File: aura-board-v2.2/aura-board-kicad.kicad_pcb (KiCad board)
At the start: 2 copper layers, 76.8 x 53.3 mm, 21 parts, among them J1 Power, J2 PWM, J3 BBCON, J4 Atto, J5 GPS, J6 SBUS, J7 Tele, J8 I2C0, U1 TSR2-2450, U2 PocketBeagle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

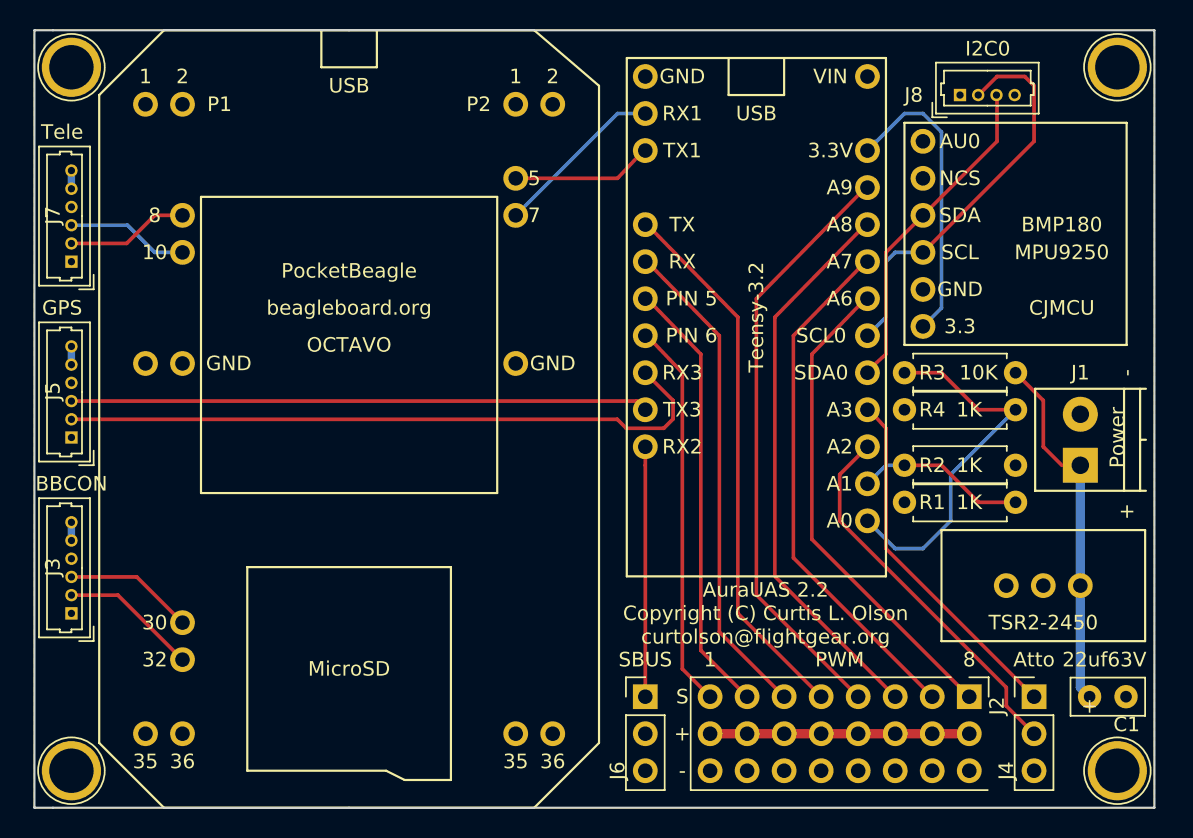
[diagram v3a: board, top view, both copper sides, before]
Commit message: Follow the standard drone-code pin order for external connectors. Fiddle with a couple traces to hopefully shorten and simplify.
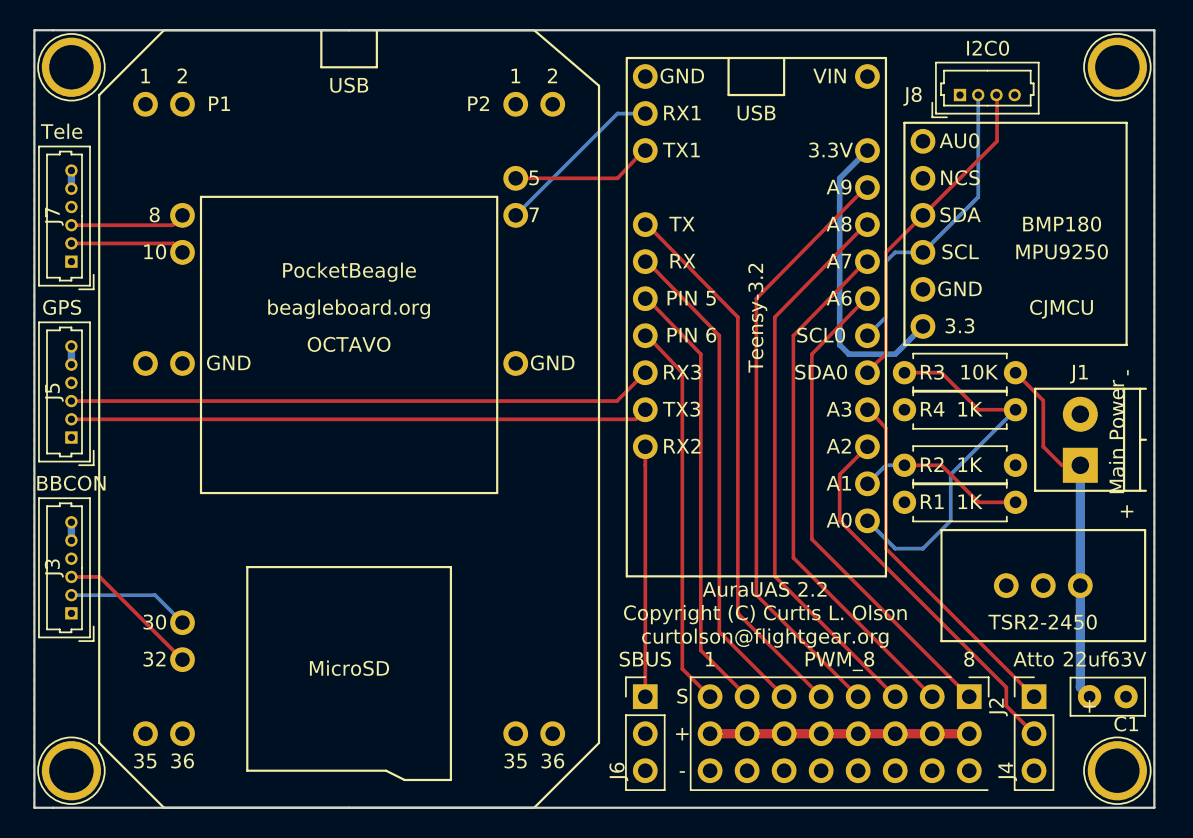
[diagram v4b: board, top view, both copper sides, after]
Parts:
- J1: value Power -> Main Power
- J2: value PWM -> PWM_8
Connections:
- J3 pad 2: /UART0_RX -> /UART0_TX
- J3 pad 3: /UART0_TX -> /UART0_RX
- J5 pad 2: /GPS_RX -> /GPS_TX
- J5 pad 3: /GPS_TX -> /GPS_RX
- J7 pad 2: /UART2_RX -> /UART2_TX
- J7 pad 3: /UART2_TX -> /UART2_RX
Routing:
- net /I2C0_SCL: track 27.6 -> 20.8 mm
- net /GPS_RX: track 45.9 -> 40.3 mm
- net /UART2_RX: track 8.42 -> 7.90 mm
- net /UART2_TX: track 8.39 -> 7.87 mm
- net /UART0_TX: track 8.92 -> 8.40 mm
- net /UART0_RX: track 9.45 -> 9.97 mm
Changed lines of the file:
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@@
     (thickness 1.6)
     (drawings 15)
-    (tracks 119)
+    (tracks 109)
     (zones 0)
     (modules 21)
@@
   )
   (setup
-    (last_trace_width 0.1524)
+    (last_trace_width 0.635)
     (user_trace_width 0.254)
     (user_trace_width 0.381)
@@
       (net 11 +5V))
     (pad 2 thru_hole circle (at 1.25 0 90) (size 0.85 0.85) (drill 0.5) (layers *.Cu *.Mask)
+      (net 18 /GPS_TX))
+    (pad 3 thru_hole circle (at 2.5 0 90) (size 0.85 0.85) (drill 0.5) (layers *.Cu *.Mask)
       (net 17 /GPS_RX))
-    (pad 3 thru_hole circle (at 2.5 0 90) (size 0.85 0.85) (drill 0.5) (layers *.Cu *.Mask)
-      (net 18 /GPS_TX))
     (pad 4 thru_hole circle (at 3.75 0 90) (size 0.85 0.85) (drill 0.5) (layers *.Cu *.Mask)
       (net 19 "Net-(J5-Pad4)"))
@@
       (net 11 +5V))
     (pad 2 thru_hole circle (at 1.25 0 90) (size 0.85 0.85) (drill 0.5) (layers *.Cu *.Mask)
+      (net 13 /UART0_TX))
+    (pad 3 thru_hole circle (at 2.5 0 90) (size 0.85 0.85) (drill 0.5) (layers *.Cu *.Mask)
       (net 12 /UART0_RX))
-    (pad 3 thru_hole circle (at 2.5 0 90) (size 0.85 0.85) (drill 0.5) (layers *.Cu *.Mask)
-      (net 13 /UART0_TX))
     (pad 4 thru_hole circle (at 3.75 0 90) (size 0.85 0.85) (drill 0.5) (layers *.Cu *.Mask)
       (net 14 "Net-(J3-Pad4)"))
@@
       (net 11 +5V))
     (pad 2 thru_hole circle (at 1.25 0 90) (size 0.85 0.85) (drill 0.5) (layers *.Cu *.Mask)
+      (net 22 /UART2_TX))
+    (pad 3 thru_hole circle (at 2.5 0 90) (size 0.85 0.85) (drill 0.5) (layers *.Cu *.Mask)
       (net 21 /UART2_RX))
-    (pad 3 thru_hole circle (at 2.5 0 90) (size 0.85 0.85) (drill 0.5) (layers *.Cu *.Mask)
-      (net 22 /UART2_TX))
     (pad 4 thru_hole circle (at 3.75 0 90) (size 0.85 0.85) (drill 0.5) (layers *.Cu *.Mask)
       (net 23 "Net-(J7-Pad4)"))
@@
       (effects (font (size 1 1) (thickness 0.15)))
     )
-    (fp_text value PWM (at -2.54 8.89 360) (layer F.SilkS)
+    (fp_text value PWM_8 (at -2.54 8.89 360) (layer F.SilkS)
       (effects (font (size 1 1) (thickness 0.15)))
     )
@@
       (effects (font (size 1 1) (thickness 0.15)))
     )
-    (fp_text value Power (at 1.905 2.54 90) (layer F.SilkS)
+    (fp_text value "Main Power" (at 1.905 2.54 90) (layer F.SilkS)
       (effects (font (size 1 1) (thickness 0.15)))
     )
@@
   (segment (start 92.075 95.25) (end 81.28 84.455) (width 0.25) (layer F.Cu) (net 10) (status 10))
   (segment (start 85.09 53.086) (end 85.09 52.578) (width 0.635) (layer B.Cu) (net 11) (status 30))
-  (segment (start 30.48 88.285) (end 33.675 88.285) (width 0.254) (layer F.Cu) (net 12))
-  (segment (start 33.675 88.285) (end 38.1 92.71) (width 0.254) (layer F.Cu) (net 12))
-  (segment (start 30.48 87.035) (end 34.965 87.035) (width 0.254) (layer F.Cu) (net 13))
-  (segment (start 34.965 87.035) (end 38.1 90.17) (width 0.254) (layer F.Cu) (net 13))
+  (segment (start 30.48 87.035) (end 32.425 87.035) (width 0.254) (layer F.Cu) (net 12))
+  (segment (start 32.425 87.035) (end 38.1 92.71) (width 0.254) (layer F.Cu) (net 12))
+  (segment (start 30.48 88.285) (end 36.215 88.285) (width 0.254) (layer B.Cu) (net 13))
+  (segment (start 36.215 88.285) (end 38.1 90.17) (width 0.254) (layer B.Cu) (net 13))
   (segment (start 96.52 95.25) (end 86.36 85.09) (width 0.25) (layer F.Cu) (net 15) (status 10))
   (segment (start 86.36 85.09) (end 86.36 76.835) (width 0.25) (layer F.Cu) (net 15))
@@
   (segment (start 85.09 78.105) (end 85.09 77.978) (width 0.254) (layer F.Cu) (net 16) (status 30))
   (segment (start 96.52 97.79) (end 95.885 97.79) (width 0.254) (layer F.Cu) (net 16))
-  (segment (start 69.85 73.025) (end 71.755 74.93) (width 0.254) (layer F.Cu) (net 17))
-  (segment (start 67.925 76.22) (end 30.48 76.22) (width 0.254) (layer F.Cu) (net 17))
-  (segment (start 68.54 76.835) (end 67.925 76.22) (width 0.254) (layer F.Cu) (net 17))
-  (segment (start 71.12 76.835) (end 68.54 76.835) (width 0.254) (layer F.Cu) (net 17))
-  (segment (start 71.755 76.2) (end 71.12 76.835) (width 0.254) (layer F.Cu) (net 17))
-  (segment (start 71.755 74.93) (end 71.755 76.2) (width 0.254) (layer F.Cu) (net 17))
+  (segment (start 30.48 74.97) (end 67.905 74.97) (width 0.254) (layer F.Cu) (net 17))
+  (segment (start 67.905 74.97) (end 69.85 73.025) (width 0.254) (layer F.Cu) (net 17))
   (segment (start 69.85 72.898) (end 69.85 73.025) (width 0.254) (layer F.Cu) (net 17) (status 30))
-  (segment (start 30.48 74.97) (end 69.255 74.97) (width 0.254) (layer F.Cu) (net 18))
-  (segment (start 69.255 74.97) (end 69.85 75.565) (width 0.254) (layer F.Cu) (net 18))
+  (segment (start 30.48 76.22) (end 69.195 76.22) (width 0.254) (layer F.Cu) (net 18))
+  (segment (start 69.195 76.22) (end 69.85 75.565) (width 0.254) (layer F.Cu) (net 18))
   (segment (start 69.85 79.375) (end 69.85 77.978) (width 0.25) (layer F.Cu) (net 20) (status 20))
   (segment (start 69.85 95.25) (end 69.85 79.375) (width 0.25) (layer F.Cu) (net 20))
   (segment (start 69.85 95.25) (end 69.85 95.25) (width 0.25) (layer F.Cu) (net 20))
-  (segment (start 38.1 62.23) (end 36.195 62.23) (width 0.254) (layer F.Cu) (net 21))
-  (segment (start 34.27 64.155) (end 30.48 64.155) (width 0.254) (layer F.Cu) (net 21) (status 20))
-  (segment (start 36.195 62.23) (end 34.27 64.155) (width 0.254) (layer F.Cu) (net 21))
-  (segment (start 38.1 64.77) (end 36.195 64.77) (width 0.254) (layer B.Cu) (net 22))
-  (segment (start 34.33 62.905) (end 30.48 62.905) (width 0.254) (layer B.Cu) (net 22) (status 20))
-  (segment (start 36.195 64.77) (end 34.33 62.905) (width 0.254) (layer B.Cu) (net 22))
+  (segment (start 30.48 62.905) (end 37.425 62.905) (width 0.254) (layer F.Cu) (net 21))
+  (segment (start 37.425 62.905) (end 38.1 62.23) (width 0.254) (layer F.Cu) (net 21))
+  (segment (start 30.48 64.155) (end 37.485 64.155) (width 0.254) (layer F.Cu) (net 22))
+  (segment (start 37.485 64.155) (end 38.1 64.77) (width 0.254) (layer F.Cu) (net 22))
   (segment (start 85.09 80.645) (end 86.36 79.375) (width 0.254) (layer B.Cu) (net 24))
   (segment (start 86.36 79.375) (end 87.63 79.375) (width 0.254) (layer B.Cu) (net 24))
@@
   (segment (start 86.36 64.77) (end 86.36 71.755) (width 0.25) (layer F.Cu) (net 26))
   (segment (start 86.36 71.755) (end 85.09 72.898) (width 0.25) (layer F.Cu) (net 26) (status 20))
+  (segment (start 92.69 53.975) (end 92.69 60.98) (width 0.254) (layer B.Cu) (net 27))
+  (segment (start 92.69 60.98) (end 88.9 64.77) (width 0.254) (layer B.Cu) (net 27))
   (segment (start 85.09 70.485) (end 86.36 69.215) (width 0.254) (layer B.Cu) (net 27))
+  (segment (start 86.36 69.215) (end 86.36 65.405) (width 0.254) (layer B.Cu) (net 27))
+  (segment (start 86.36 65.405) (end 86.995 64.77) (width 0.254) (layer B.Cu) (net 27))
   (segment (start 86.995 64.77) (end 88.9 64.77) (width 0.254) (layer B.Cu) (net 27))
-  (segment (start 86.36 65.405) (end 86.995 64.77) (width 0.254) (layer B.Cu) (net 27))
-  (segment (start 86.36 69.215) (end 86.36 65.405) (width 0.254) (layer B.Cu) (net 27))
-  (segment (start 88.9 64.77) (end 96.52 57.15) (width 0.254) (layer F.Cu) (net 27))
-  (segment (start 93.98 52.705) (end 92.71 53.975) (width 0.254) (layer F.Cu) (net 27))
-  (segment (start 95.885 52.705) (end 93.98 52.705) (width 0.254) (layer F.Cu) (net 27))
-  (segment (start 96.52 53.34) (end 95.885 52.705) (width 0.254) (layer F.Cu) (net 27))
-  (segment (start 96.52 57.15) (end 96.52 53.34) (width 0.254) (layer F.Cu) (net 27))
   (segment (start 92.71 53.975) (end 92.69 53.975) (width 0.254) (layer F.Cu) (net 27))
   (segment (start 89.535 97.79) (end 92.075 97.79) (width 0.635) (layer F.Cu) (net 28))
@@
   (segment (start 67.945 55.245) (end 69.85 55.245) (width 0.254) (layer B.Cu) (net 30))
   (segment (start 60.96 62.23) (end 61.595 62.23) (width 0.254) (layer B.Cu) (net 30))
-  (segment (start 88.9 69.85) (end 90.17 68.58) (width 0.254) (layer B.Cu) (net 31))
-  (segment (start 87.63 55.245) (end 85.09 57.785) (width 0.254) (layer B.Cu) (net 31))
-  (segment (start 88.9 55.245) (end 87.63 55.245) (width 0.254) (layer B.Cu) (net 31))
-  (segment (start 90.17 56.515) (end 88.9 55.245) (width 0.254) (layer B.Cu) (net 31))
-  (segment (start 90.17 68.58) (end 90.17 56.515) (width 0.254) (layer B.Cu) (net 31))
-  (segment (start 85.598 57.15) (end 85.09 57.658) (width 0.254) (layer B.Cu) (net 31) (status 30))
+  (segment (start 88.9 69.85) (end 86.995 71.755) (width 0.381) (layer B.Cu) (net 31))
+  (segment (start 83.185 59.69) (end 85.09 57.785) (width 0.381) (layer B.Cu) (net 31))
+  (segment (start 83.185 71.12) (end 83.185 59.69) (width 0.381) (layer B.Cu) (net 31))
+  (segment (start 83.82 71.755) (end 83.185 71.12) (width 0.381) (layer B.Cu) (net 31))
+  (segment (start 86.995 71.755) (end 83.82 71.755) (width 0.381) (layer B.Cu) (net 31))
   (zone (net 2) (net_name GND) (layer B.Cu) (hatch edge 0.508)
     (connect_pads (clearance 0.508))
